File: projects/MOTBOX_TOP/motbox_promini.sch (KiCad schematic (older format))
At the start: 28 parts, among them J19 Open Close Done, J20 Motor, J3 12V IN, J4 Manual EN, J5 OBS_IR_TX, J6 OP_CL_OBS_DET_LED, J7 OBS IR RX, P1 Digital, P2 ADC, P3 COM, P4 ADC, P5 Analog, U1 LM2575-5.0BU, U2 LM393, U3 L293D

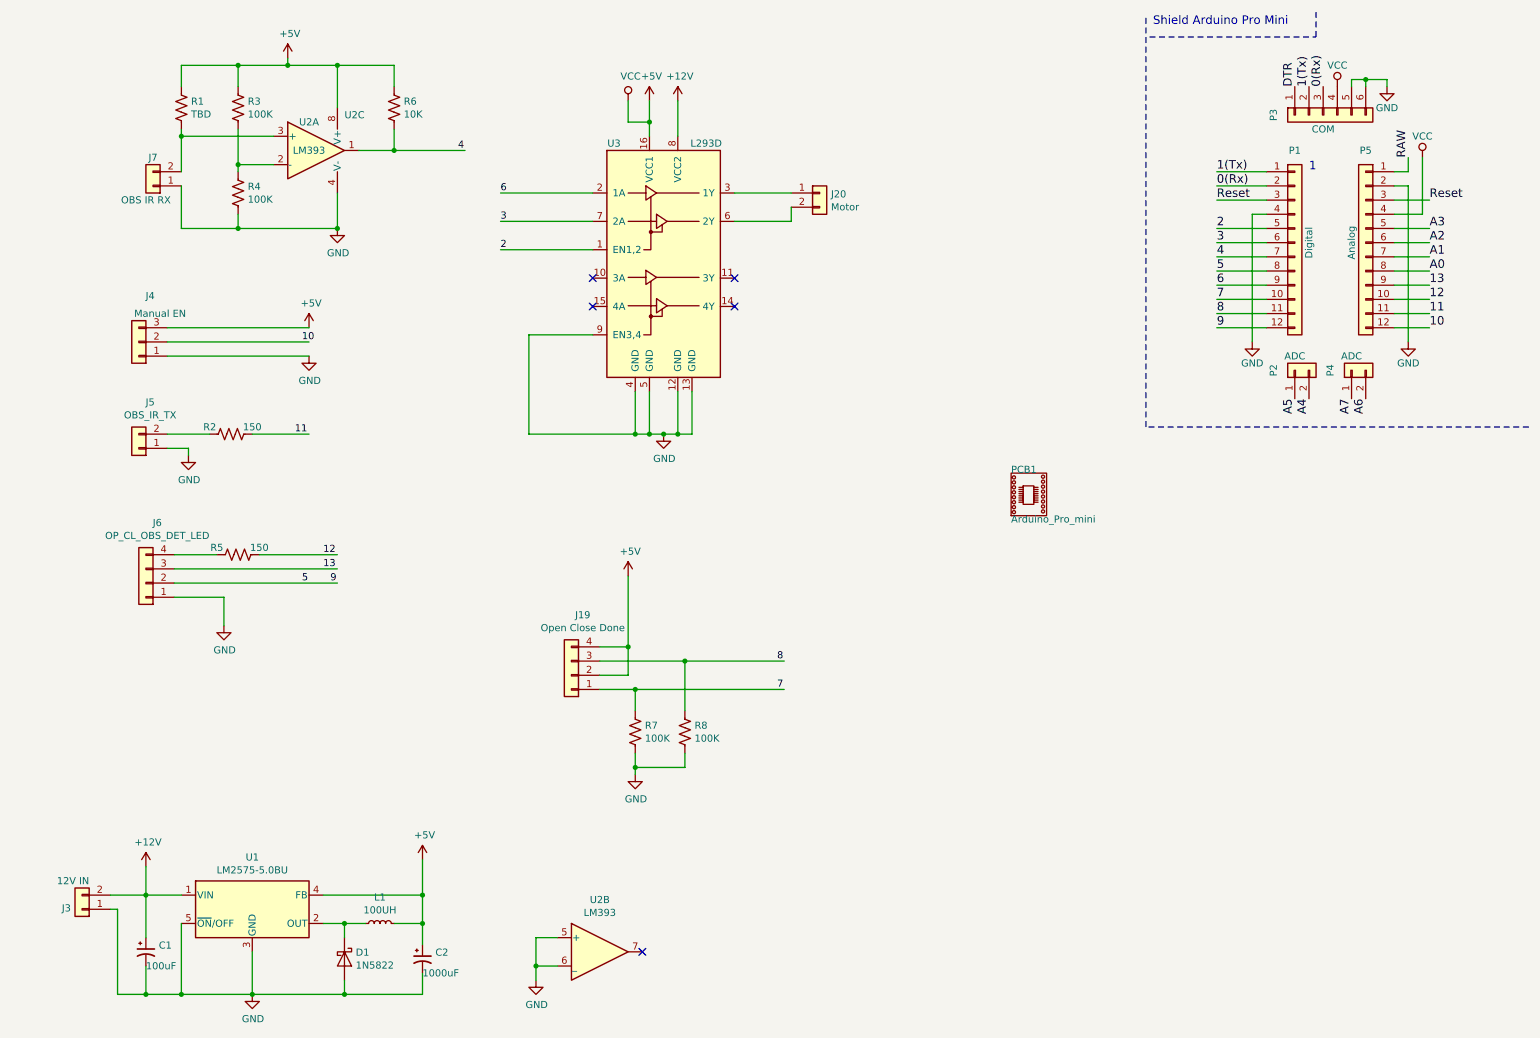
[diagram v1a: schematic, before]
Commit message: New library files and schematics with ESE31 and DT045 switches
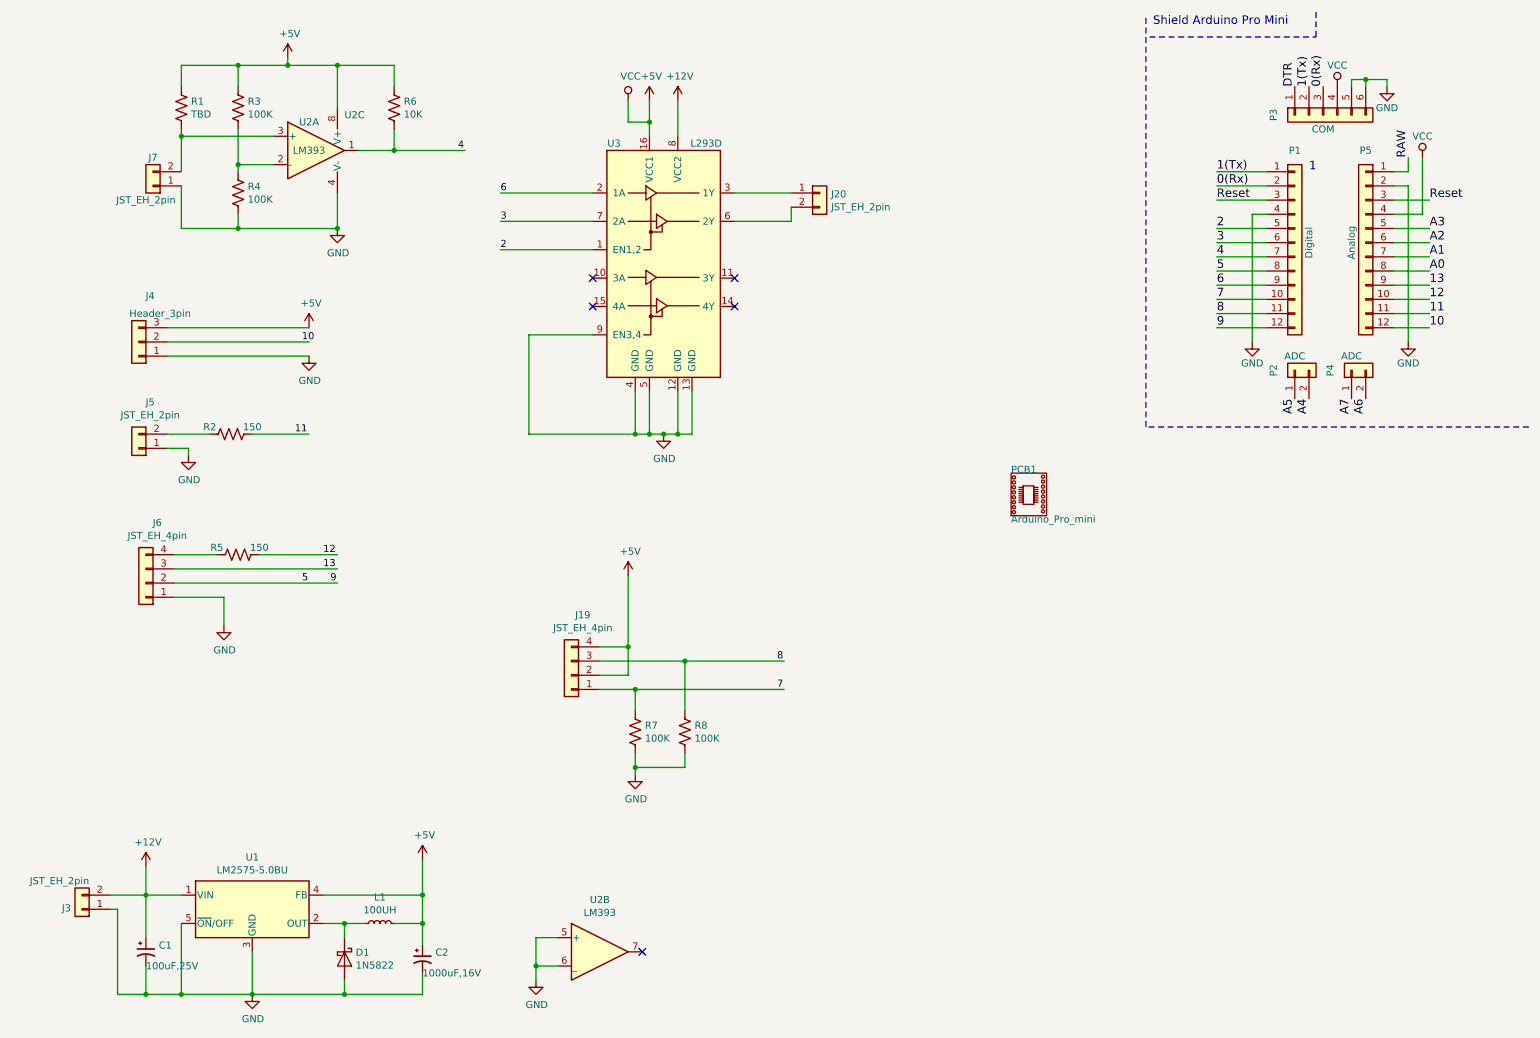
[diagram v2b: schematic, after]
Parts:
- C1: value 100uF -> 100uF,25V
- C2: value 1000uF -> 1000uF,16V
- J19: value Open Close Done -> JST_EH_4pin
- J20: value Motor -> JST_EH_2pin
- J3: value 12V IN -> JST_EH_2pin
- J4: value Manual EN -> Header_3pin
- J5: value OBS_IR_TX -> JST_EH_2pin
- J6: value OP_CL_OBS_DET_LED -> JST_EH_4pin
- J7: value OBS IR RX -> JST_EH_2pin
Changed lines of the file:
@@
 AR Path="/5CCC7C1B/5CC2F2EA" Ref="J7"  Part="1"
 F 0 "J7" H 1500 1550 50  0000 C CNN
-F 1 "OBS IR RX" H 1550 1850 50  0000 C CNN
+F 1 "JST_EH_2pin" H 1550 1850 50  0000 C CNN
 F 2 "Connector_JST:JST_EH_B02B-EH-A_1x02_P2.50mm_Vertical" H 1500 1750 50  0001 C CNN
 F 3 "~" H 1500 1750 50  0001 C CNN
@@
 AR Path="/5CCC7C1B/5CC2F2FF" Ref="J20"  Part="1"
 F 0 "J20" H 6280 1792 50  0000 L CNN
-F 1 "Motor" H 6280 1701 50  0000 L CNN
+F 1 "JST_EH_2pin" H 6280 1701 50  0000 L CNN
 F 2 "Connector_JST:JST_EH_B02B-EH-A_1x02_P2.50mm_Vertical" H 6200 1800 50  0001 C CNN
 F 3 "~" H 6200 1800 50  0001 C CNN
@@
 AR Path="/5CCC7C1B/5CC2F306" Ref="J19"  Part="1"
 F 0 "J19" H 4370 4775 50  0000 C CNN
-F 1 "Open Close Done" H 4370 4866 50  0000 C CNN
+F 1 "JST_EH_4pin" H 4370 4866 50  0000 C CNN
 F 2 "Connector_JST:JST_EH_B04B-EH-A_1x04_P2.50mm_Vertical" H 4450 5200 50  0001 C CNN
 F 3 "~" H 4450 5200 50  0001 C CNN
@@
 AR Path="/5CCC7C1B/5CC2F314" Ref="C1"  Part="1"
 F 0 "C1" H 1541 7196 50  0000 L CNN
-F 1 "100uF" H 1450 7050 50  0000 L CNN
+F 1 "100uF,25V" H 1450 7050 50  0000 L CNN
 F 2 "Capacitor_SMD:CP_Elec_6.3x7.7" H 1450 7150 50  0001 C CNN
 F 3 "~" H 1450 7150 50  0001 C CNN
@@
 AR Path="/5CCC7C1B/5CC2F31B" Ref="C2"  Part="1"
 F 0 "C2" H 3491 7246 50  0000 L CNN
-F 1 "1000uF" H 3400 7100 50  0000 L CNN
+F 1 "1000uF,16V" H 3400 7100 50  0000 L CNN
 F 2 "Capacitor_SMD:CP_Elec_10x10" H 3400 7200 50  0001 C CNN
 F 3 "~" H 3400 7200 50  0001 C CNN
@@
 AR Path="/5CCC7C1B/5CC2F337" Ref="J3"  Part="1"
 F 0 "J3" H 1079 6842 50  0000 L CNN
-F 1 "12V IN" H 950 6650 50  0000 L CNN
+F 1 "JST_EH_2pin" H 950 6650 50  0000 L CNN
 F 2 "Connector_JST:JST_EH_B02B-EH-A_1x02_P2.50mm_Vertical" H 1000 6850 50  0001 C CNN
 F 3 "~" H 1000 6850 50  0001 C CNN
@@
 AR Path="/5CCC7C1B/5CC2F3B4" Ref="J4"  Part="1"
 F 0 "J4" H 1320 2525 50  0000 C CNN
-F 1 "Manual EN" H 1250 2650 50  0000 C CNN
+F 1 "Header_3pin" H 1250 2650 50  0000 C CNN
 F 2 "Connector_PinHeader_2.54mm:PinHeader_1x03_P2.54mm_Vertical" H 1400 2850 50  0001 C CNN
 F 3 "~" H 1400 2850 50  0001 C CNN
@@
 P 1400 3600
 F 0 "J5" H 1320 3275 50  0000 C CNN
-F 1 "OBS_IR_TX" H 1320 3366 50  0000 C CNN
+F 1 "JST_EH_2pin" H 1320 3366 50  0000 C CNN
 F 2 "Connector_JST:JST_EH_B02B-EH-A_1x02_P2.50mm_Vertical" H 1400 3600 50  0001 C CNN
 F 3 "~" H 1400 3600 50  0001 C CNN
@@
 AR Path="/5CCC7C1B/5CC122C9" Ref="J6"  Part="1"
 F 0 "J6" H 1370 4125 50  0000 C CNN
-F 1 "OP_CL_OBS_DET_LED" H 1370 4216 50  0000 C CNN
+F 1 "JST_EH_4pin" H 1370 4216 50  0000 C CNN
 F 2 "Connector_JST:JST_EH_B04B-EH-A_1x04_P2.50mm_Vertical" H 1450 4550 50  0001 C CNN
 F 3 "~" H 1450 4550 50  0001 C CNN
